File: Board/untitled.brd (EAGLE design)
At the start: 100 x 80 mm, 48 parts, among them IC2 MEGA16-A, Q1 8 MHz

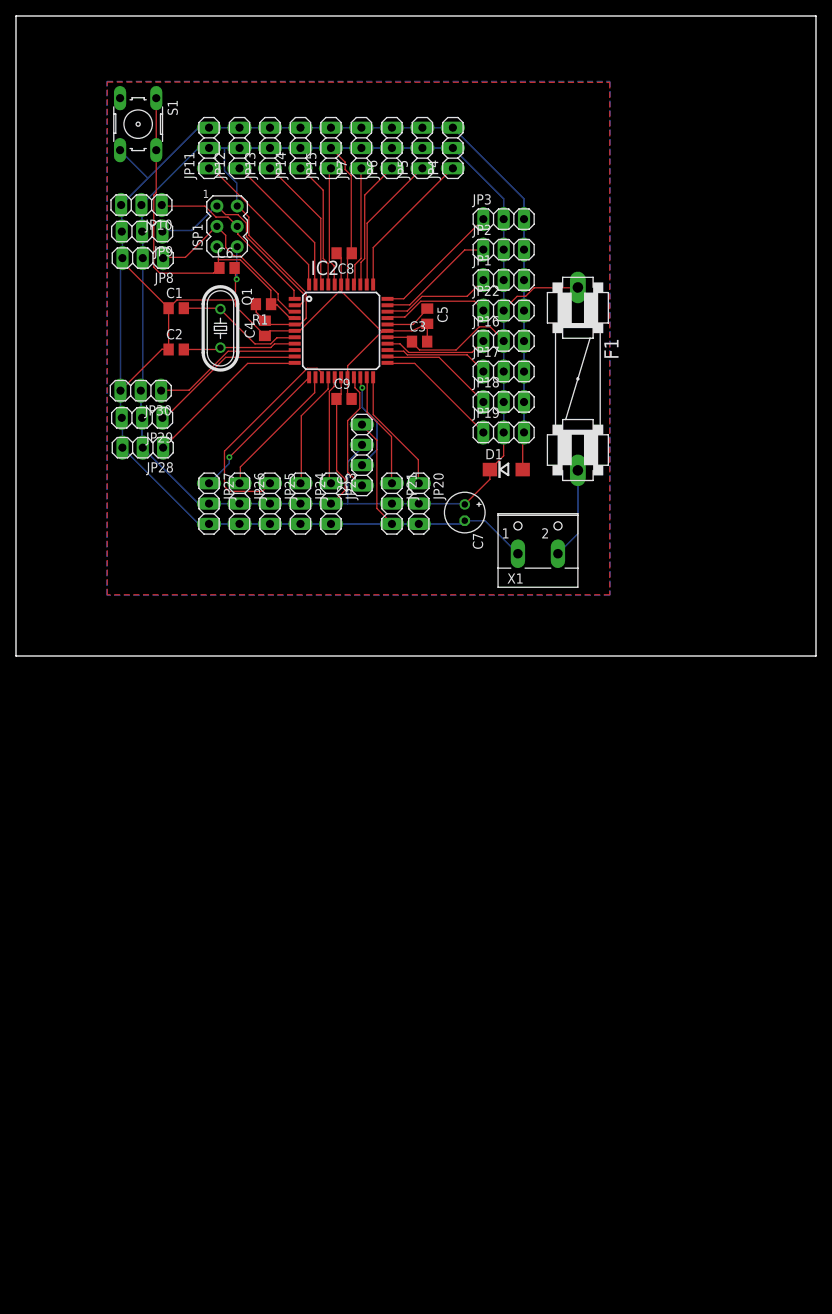
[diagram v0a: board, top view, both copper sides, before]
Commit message: Seperate power input fot uC and servos. Change uC rom QFP to DIP for better repair process.
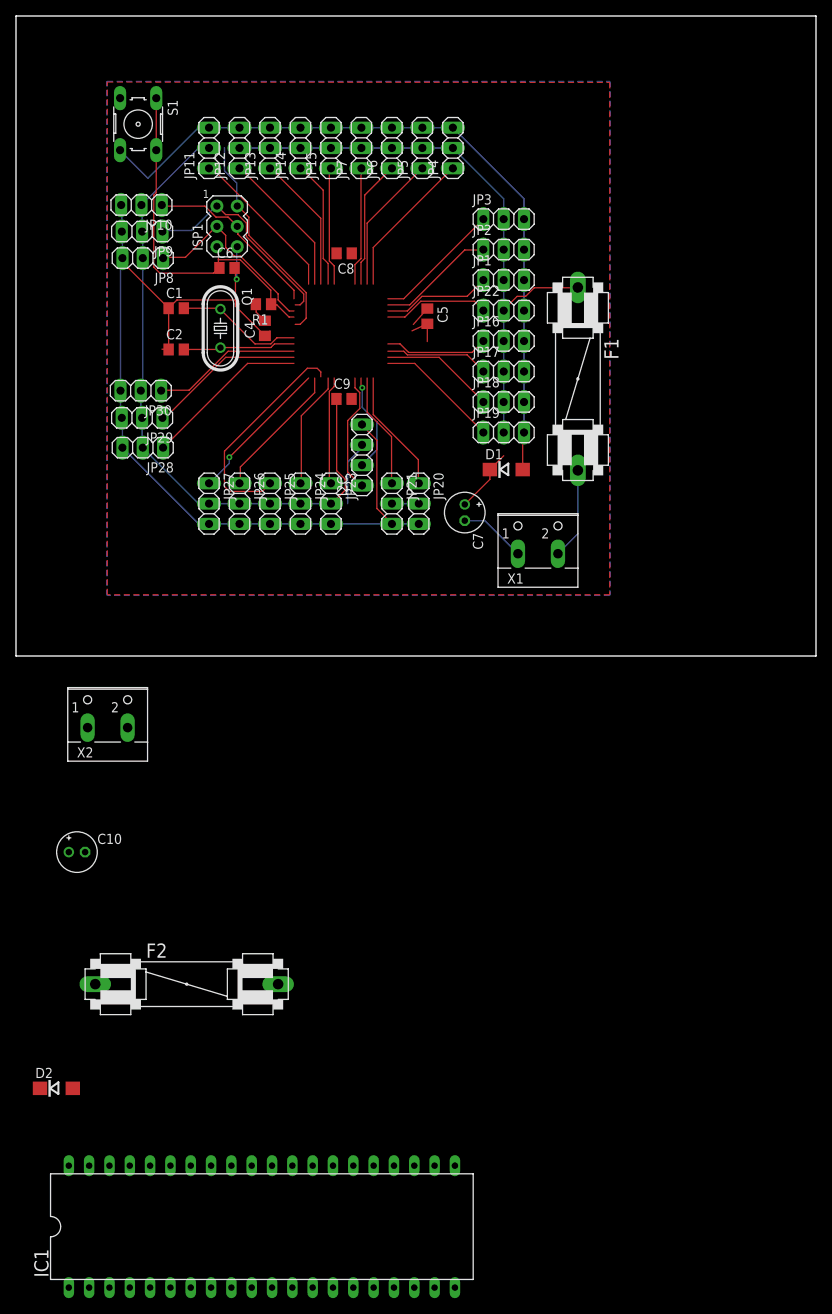
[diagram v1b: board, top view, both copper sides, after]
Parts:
- removed C3: 100 nF, rcl:C0805
- removed IC2: MEGA16-A, atmel:TQFP44
- added C10: 1000 uF, rcl:E2-5
- added D2: 1N4004, diode:DO214AC
- added F2: 3A 125VAC 125VDC, special:FUSE
- added IC1: MEGA16-P, atmel:DIL40
- added X2: (no value), con-wago-500:W237-102
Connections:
- new net N$9: F2.2, X2.2
- net GND: now also C10.-, D2.A, IC1.11, IC1.31, X2.1; no longer C3.2, IC2.18, IC2.28, IC2.39, IC2.6
- net N$1: now also IC1.12; no longer IC2.7
- net N$13: now also IC1.36; no longer IC2.33
- net N$15: now also IC1.33; no longer IC2.30
- net N$16: now also IC1.39; no longer IC2.36
- net N$2: now also IC1.13; no longer IC2.8
- net N$21: now also IC1.28; no longer IC2.25
- net N$22: now also IC1.7; no longer IC2.2
- net N$23: now also IC1.27; no longer IC2.24
- net N$24: now also IC1.40; no longer IC2.37
- net N$25: now also IC1.4; no longer IC2.43
- net N$27: now also IC1.29; no longer IC2.26
- net N$29: now also IC1.2; no longer IC2.41
- net N$3: now also IC1.32; no longer IC2.29
- net N$30: now also IC1.3; no longer IC2.42
- net N$31: now also IC1.37; no longer IC2.34
- net N$32: now also IC1.5; no longer IC2.44
- net N$33: now also IC1.23; no longer IC2.20
- net N$34: now also IC1.22; no longer IC2.19
- net N$36: now also IC1.38; no longer IC2.35
- net N$39: now also IC1.35; no longer IC2.32
- net N$40: now also IC1.34; no longer IC2.31
- net N$41: now also IC1.26; no longer IC2.23
- net N$42: now also IC1.25; no longer IC2.22
- net N$43: now also IC1.24; no longer IC2.21
- net N$44: now also IC1.21; no longer IC2.16
- net N$45: now also IC1.20; no longer IC2.15
- net N$46: now also IC1.19; no longer IC2.14
- net N$47: now also IC1.18; no longer IC2.13
- net N$48: now also IC1.17; no longer IC2.12
- net N$49: now also IC1.16; no longer IC2.11
- net N$5: now also IC1.8; no longer IC2.3
- net N$56: now also IC1.15; no longer IC2.10
- net N$57: now also IC1.14; no longer IC2.9
- net N$6: now also IC1.6; no longer IC2.1
- net N$7: now also IC1.9; no longer IC2.4
- net N$8: now also IC1.1; no longer IC2.40
- net VCC: now also C10.+, D2.C, F2.1, IC1.10, IC1.30; no longer C3.1, IC2.17, IC2.27, IC2.38, IC2.5
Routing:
- net VCC: track 270.8 -> 209.3 mm
- net GND: track 285.3 -> 229.2 mm
- net N$3: track 5.87 -> 2.65 mm

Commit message: Create new board
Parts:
- moved IC1 114.8 mm to (55.9, 40.6), turned to 270 degrees
- moved D2 80.7 mm to (15.2, 26.0), turned to 270 degrees
- moved F2 68.1 mm to (9.53, 26.0), turned to 270 degrees
- moved C10 52.0 mm to (19.7, 26.0), turned to 270 degrees
- moved ISP1 40.6 mm to (61.0, 74.9), turned to 90 degrees
- moved S1 34.9 mm to (49.5, 73.0)
- moved JP23 34.7 mm to (73.7, 14.0), turned to 0 degrees
- moved JP7 32.1 mm to (73.7, 73.7), turned to 0 degrees
- moved C8 30.0 mm to (23.5, 26.0), turned to 90 degrees
- moved JP6 27.4 mm to (73.7, 69.8), turned to 0 degrees
- moved C9 27.3 mm to (67.3, 39.4), turned to 180 degrees
- moved JP21 26.7 mm to (73.7, 17.8), turned to 0 degrees
- moved C7 25.9 mm to (80.6, 26.0)
- moved D1 24.0 mm to (85.1, 26.0), turned to 270 degrees
- moved X1 23.7 mm to (88.3, 8.26)
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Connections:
- removed net N$33: I2C.2, IC1.23
- removed net N$34: I2C.1, IC1.22
- new net +5V: C10.+, C8.2, D2.C, F2.1, JP1.2, JP10.2, JP11.2, JP12.2, JP13.2, JP14.2, JP15.2, JP16.2, JP17.2, JP18.2, JP19.2, JP2.2, JP20.2, JP21.2, JP22.2, JP23.2, JP24.2, JP25.2, JP26.2, JP27.2, JP28.2, JP29.2, JP3.2, JP30.2, JP4.2, JP5.2, JP6.2, JP7.2, JP8.2, JP9.2
- new net N$10: F2.2, X2.1
- new net N$17: I2C.3, IC1.23
- net GND: now also C8.1, C9.1, I2C.1, X2.2; no longer C8.2, C9.2, I2C.4, X2.1
- net N$9: now also I2C.4, IC1.22; no longer F2.2, X2.2
- net VCC: now also C9.2, I2C.2; no longer C10.+, C8.1, C9.1, D2.C, F2.1, I2C.3, JP1.2, JP10.2, JP11.2, JP12.2, JP13.2, JP14.2, JP15.2, JP16.2, JP17.2, JP18.2, JP19.2, JP2.2, JP20.2, JP21.2, JP22.2, JP23.2, JP24.2, JP25.2, JP26.2, JP27.2, JP28.2, JP29.2, JP3.2, JP30.2, JP4.2, JP5.2, JP6.2, JP7.2, JP8.2, JP9.2
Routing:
- net +5V: track 0.00 -> 220.2 mm
- net GND: track 229.2 -> 389.2 mm, vias 1 -> 0
- net VCC: track 209.3 -> 138.7 mm
- net N$6: track 22.6 -> 47.0 mm
- net N$5: track 23.7 -> 47.0 mm
- net N$22: track 26.7 -> 44.1 mm
- net N$34: track 15.1 -> 0.00 mm
- net N$17: track 0.00 -> 14.0 mm
- net N$33: track 12.5 -> 0.00 mm, vias 1 -> 0
- net N$9: track 0.00 -> 10.4 mm
- net N$46: track 27.9 -> 17.9 mm
- net N$31: track 18.6 -> 9.72 mm
- net N$7: track 46.2 -> 54.4 mm
- net N$10: track 0.00 -> 7.64 mm
- net N$36: track 17.4 -> 10.3 mm
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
